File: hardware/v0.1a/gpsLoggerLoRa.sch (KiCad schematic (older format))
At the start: 34 parts, among them P1 USB_OTG, P2 CONN_01X02, Q2 FG6943010R, SW1 SW_PUSH, U2 MCP73812, U6 TPS78230

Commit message: Fixing up some errors after shuffle of libraries.
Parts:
- removed C11, C14, C6, C9: 100n, Capacitors_SMD:C_0603, symbol device:C
- removed C15, C16, C17: 1uF, Capacitors_SMD:C_0603, symbol device:C
- removed C2, C3: 22p, Capacitors_SMD:C_0603, symbol device:C
- removed D1, D2: Led_RGB_CA, footprints:LITEON_RGB, symbol gpsLogger-rescue:Led_RGB_CA
- removed FB1: 1k FB, Resistors_SMD:R_0603, symbol gpsLogger-rescue:FILTER
- removed P1: USB_OTG, footprints:USB_VERT, symbol gpsLogger-rescue:USB_OTG
- removed P2: CONN_01X02, footprints:BM02B-GHS-TBT, symbol gpsLogger-rescue:CONN_01X02
- removed Q2: FG6943010R, TO_SOT_Packages_SMD:SC-70-6, symbol gpsLogger:FG6943010R
- removed R1, R2: 27R, Resistors_SMD:R_0603, symbol device:R
- removed R10, R16, R17, R18, R19, R20, R21, R7: 1k, Resistors_SMD:R_0603, symbol device:R
- removed R12, R15: 10k, Resistors_SMD:R_0603, symbol device:R
- removed R13, R14: 100k, Resistors_SMD:R_0603, symbol device:R
- removed SW1: SW_PUSH, cameraTrigger_rev1_0:EVQ_switch, symbol gpsLogger-rescue:SW_PUSH
- removed TAG1: TAG_CONNECT, lib:tag_connect, symbol gpsLogger:TAG_CONNECT
- removed U2: MCP73812, TO_SOT_Packages_SMD:SOT-23-5, symbol gpsLogger:MCP73812
- removed U6: TPS78230, TO_SOT_Packages_SMD:SOT-23-5, symbol gpsLogger:TPS78230
- added J?: USB_OTG, symbol conn:USB_OTG
- added L?: 1k, symbol device:Ferrite_Bead_Small
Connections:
- net labels removed: +3.3V, +BATT, 1v8, LED_A_B, LED_A_G, LED_A_R, LED_B_B, LED_B_G, LED_B_R, PWR_BUT, RST, SENSE_EN, TEST, USB_IN_N, USB_IN_P, VUSB, V_SENSE, ~CHG
- wire segments 106 -> 12
- no-connect marks 1 -> 0
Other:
- note removed: "TODO: Check R7 Value\n(Charge Current)"

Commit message: Changed USB connector. Updated board outline. Updates to footprints to use 3d models. Add FLASH memory.
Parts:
- removed C1: 10n, Capacitors_SMD:C_0603, symbol device:C
- removed J?: USB_OTG, symbol conn:USB_OTG
- removed L?: 1k, symbol device:Ferrite_Bead_Small
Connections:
- net labels removed: GND, USB_DATA_N, USB_DATA_P, VBUS
- wire segments 12 -> 2
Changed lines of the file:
@@
 $Descr A3 16535 11693
 encoding utf-8
-Sheet 1 2
+Sheet 1 4
 Title "gpsLoggerLora"
 Date "2018-12-27"
@@
 Comment4 "Simple GPS logger with low power features"
 $EndDescr
-Text Label 3050 2900 0    60   ~ 0
-USB_DATA_N
-Text Label 3050 2800 0    60   ~ 0
-USB_DATA_P
 $Sheet
-S 3900 2400 2650 3400
+S 6600 2400 2650 3400
 U 5C2B8DA0
 F0 "SAMR34" 60
 F1 "SAMR34.sch" 60
-F2 "USB_DATA_N" I L 3900 2900 60
-F3 "USB_DATA_P" I L 3900 2800 60
+F2 "USB_DATA_N" I L 6600 2900 60
+F3 "USB_DATA_P" I L 6600 2800 60
+$EndSheet
+$Sheet
+S 3750 2400 2150 2150
+U 5C25E3B0
+F0 "USB" 60
+F1 "USB.sch" 60
+F2 "USB_DATA_P" I R 5900 2800 60
+F3 "USB_DATA_N" I R 5900 2900 60
+F4 "CHARGE_STAT" I R 5900 3100 60
 $EndSheet
 Wire Wire Line
-	3000 2250 3400 2250
-Text Label 3400 2250 2    60   ~ 0
-VBUS
-$Comp
-L device:C C1
-U 1 1 5691D5EA
-P 2600 3450
-F 0 "C1" H 2625 3550 50  0000 L CNN
-F 1 "10n" H 2625 3350 50  0000 L CNN
-F 2 "Capacitors_SMD:C_0603" H 2638 3300 30  0001 C CNN
-F 3 "" H 2600 3450 60  0000 C CNN
-	1    2600 3450
-	1    0    0    -1
-$EndComp
-$Comp
-L conn:USB_OTG J?
-U 1 1 5C24E04F
-P 2050 2800
-F 0 "J?" H 2105 3267 50  0000 C CNN
-F 1 "USB_OTG" H 2105 3176 50  0000 C CNN
-F 2 "" H 2200 2750 50  0001 C CNN
-F 3 "" H 2200 2750 50  0001 C CNN
-	1    2050 2800
-	1    0    0    -1
-$EndComp
-$Comp
-L device:Ferrite_Bead_Small L?
-U 1 1 5C25683B
-P 2900 2250
-F 0 "L?" V 2663 2250 50  0000 C CNN
-F 1 "1k" V 2754 2250 50  0000 C CNN
-F 2 "" V 2830 2250 50  0001 C CNN
-F 3 "~" H 2900 2250 50  0001 C CNN
-	1    2900 2250
-	0    1    1    0
-$EndComp
+	5900 2800 6600 2800
 Wire Wire Line
-	2350 2600 2600 2600
-Wire Wire Line
-	2600 2600 2600 2250
-Wire Wire Line
-	2600 2250 2800 2250
-Wire Wire Line
-	2350 2800 3900 2800
-Wire Wire Line
-	2350 2900 3900 2900
-Wire Wire Line
-	2600 3300 2600 2600
-Connection ~ 2600 2600
-$Comp
-L power:GND #PWR?
-U 1 1 5C53E1A5
-P 2600 3700
-F 0 "#PWR?" H 2600 3450 50  0001 C CNN
-F 1 "GND" H 2603 3574 50  0000 C CNN
-F 2 "" H 2500 3350 50  0001 C CNN
-F 3 "" H 2600 3700 50  0001 C CNN
-	1    2600 3700
-	1    0    0    -1
-$EndComp
-Wire Wire Line
-	2600 3700 2600 3600
-$Comp
-L power:GND #PWR?
-U 1 1 5C53E215
-P 2050 3700
-F 0 "#PWR?" H 2050 3450 50  0001 C CNN
-F 1 "GND" H 2053 3574 50  0000 C CNN
-F 2 "" H 1950 3350 50  0001 C CNN
-F 3 "" H 2050 3700 50  0001 C CNN
-	1    2050 3700
-	1    0    0    -1
-$EndComp
-Wire Wire Line
-	1950 3200 1950 3350
-Wire Wire Line
-	1950 3350 2050 3350
-Wire Wire Line
-	2050 3350 2050 3700
-Wire Wire Line
-	2050 3200 2050 3350
-Connection ~ 2050 3350
+	6600 2900 5900 2900
+$Sheet
+S 9500 2400 2850 3400
+U 5C4D6439
+F0 "memio" 60
+F1 "memio.sch" 60
+$EndSheet
 $EndSCHEMATC

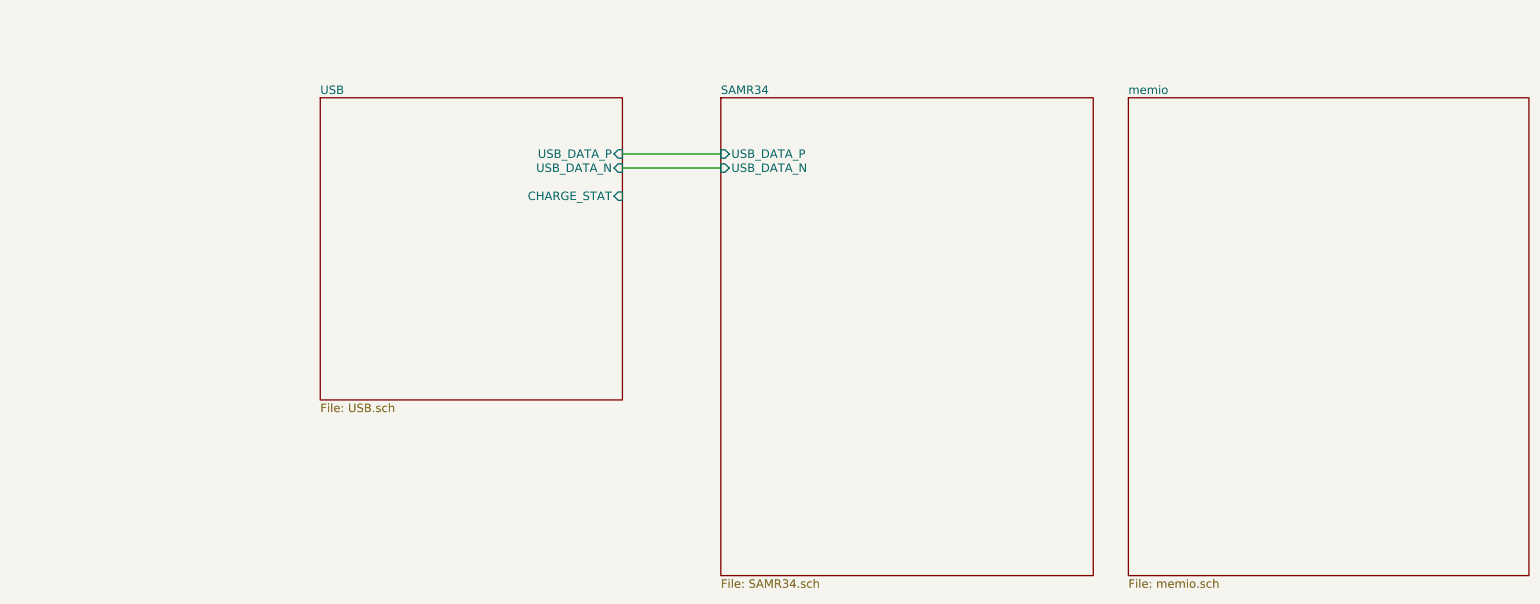
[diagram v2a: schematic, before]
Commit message: First pass schematic done. Begin routing main board.
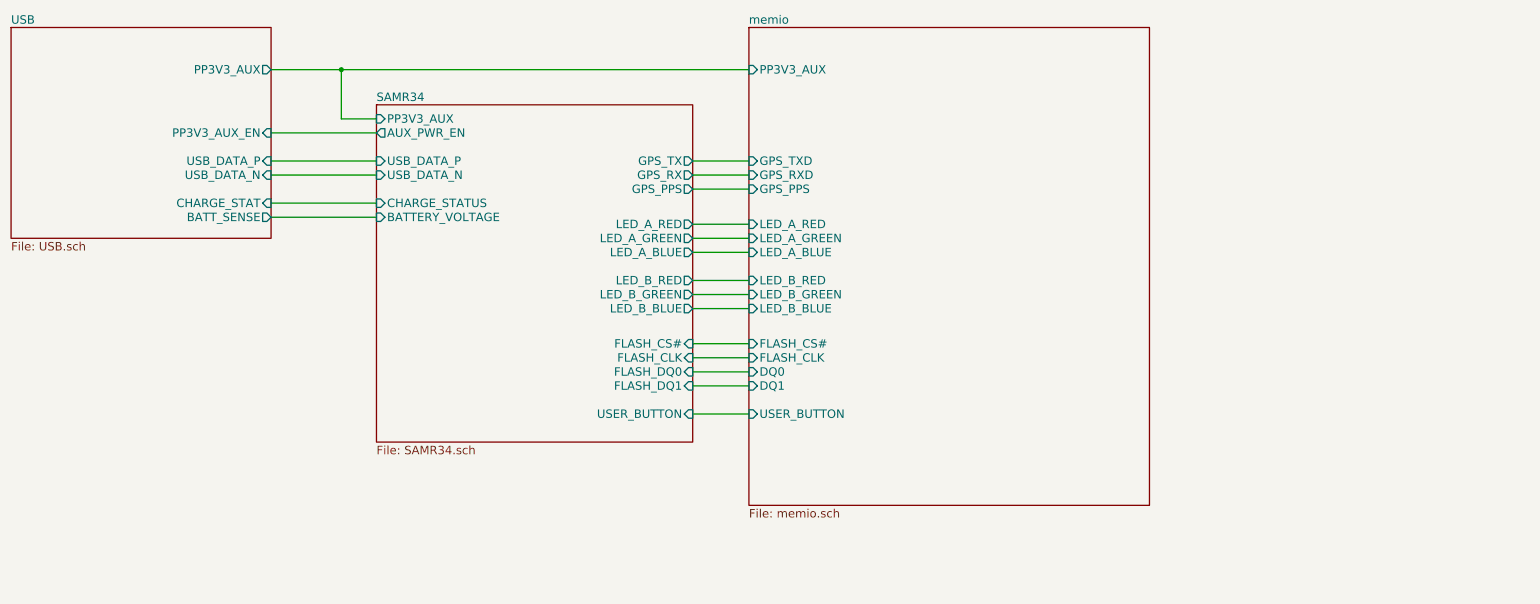
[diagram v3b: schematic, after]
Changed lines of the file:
@@
 EELAYER 26 0
 EELAYER END
-$Descr A3 16535 11693
+$Descr A4 11693 8268
 encoding utf-8
 Sheet 1 4
@@
 $EndDescr
 $Sheet
-S 6600 2400 2650 3400
+S 4150 2450 2250 2400
 U 5C2B8DA0
 F0 "SAMR34" 60
 F1 "SAMR34.sch" 60
-F2 "USB_DATA_N" I L 6600 2900 60
-F3 "USB_DATA_P" I L 6600 2800 60
+F2 "USB_DATA_N" I L 4150 2950 60
+F3 "USB_DATA_P" I L 4150 2850 60
+F4 "GPS_TX" O R 6400 2850 60
+F5 "GPS_RX" O R 6400 2950 60
+F6 "GPS_PPS" O R 6400 3050 60
+F7 "LED_A_RED" O R 6400 3300 60
+F8 "LED_A_GREEN" O R 6400 3400 60
+F9 "LED_A_BLUE" O R 6400 3500 60
+F10 "LED_B_RED" O R 6400 3700 60
+F11 "LED_B_GREEN" O R 6400 3800 60
+F12 "LED_B_BLUE" O R 6400 3900 60
+F13 "AUX_PWR_EN" O L 4150 2650 60
+F14 "FLASH_CS#" I R 6400 4150 60
+F15 "FLASH_DQ0" I R 6400 4350 60
+F16 "FLASH_DQ1" I R 6400 4450 60
+F17 "FLASH_CLK" I R 6400 4250 60
+F18 "USER_BUTTON" I R 6400 4650 60
+F19 "CHARGE_STATUS" I L 4150 3150 60
+F20 "BATTERY_VOLTAGE" I L 4150 3250 60
+F21 "PP3V3_AUX" I L 4150 2550 60
 $EndSheet
 $Sheet
-S 3750 2400 2150 2150
+S 1550 1900 1850 1500
 U 5C25E3B0
 F0 "USB" 60
 F1 "USB.sch" 60
-F2 "USB_DATA_P" I R 5900 2800 60
-F3 "USB_DATA_N" I R 5900 2900 60
-F4 "CHARGE_STAT" I R 5900 3100 60
+F2 "USB_DATA_P" I R 3400 2850 60
+F3 "USB_DATA_N" I R 3400 2950 60
+F4 "CHARGE_STAT" I R 3400 3150 60
+F5 "PP3V3_AUX_EN" I R 3400 2650 60
+F6 "PP3V3_AUX" O R 3400 2200 60
+F7 "BATT_SENSE" O R 3400 3250 60
 $EndSheet
 Wire Wire Line
-	5900 2800 6600 2800
+	3400 2850 4150 2850
 Wire Wire Line
-	6600 2900 5900 2900
+	4150 2950 3400 2950
+Wire Wire Line
+	6400 2850 6800 2850
+Wire Wire Line
+	6400 2950 6800 2950
+Wire Wire Line
+	6400 3050 6800 3050
+Wire Wire Line
+	6400 3300 6800 3300
+Wire Wire Line
+	6400 3400 6800 3400
+Wire Wire Line
+	6400 3500 6800 3500
+Wire Wire Line
+	6400 3700 6800 3700
+Wire Wire Line
+	6400 3800 6800 3800
+Wire Wire Line
+	6400 3900 6800 3900
+Wire Wire Line
+	4150 2650 3400 2650
 $Sheet
-S 9500 2400 2850 3400
+S 6800 1900 2850 3400
 U 5C4D6439
 F0 "memio" 60
 F1 "memio.sch" 60
+F2 "GPS_TXD" I L 6800 2850 60
+F3 "GPS_RXD" I L 6800 2950 60
+F4 "GPS_PPS" I L 6800 3050 60
+F5 "LED_A_RED" I L 6800 3300 60
+F6 "LED_A_GREEN" I L 6800 3400 60
+F7 "LED_A_BLUE" I L 6800 3500 60
+F8 "LED_B_RED" I L 6800 3700 60
+F9 "LED_B_GREEN" I L 6800 3800 60
+F10 "LED_B_BLUE" I L 6800 3900 60
+F11 "DQ0" I L 6800 4350 60
+F12 "DQ1" I L 6800 4450 60
+F13 "FLASH_CLK" I L 6800 4250 60
+F14 "FLASH_CS#" I L 6800 4150 60
+F15 "PP3V3_AUX" I L 6800 2200 60
+F16 "USER_BUTTON" I L 6800 4650 60
 $EndSheet
+Wire Wire Line
+	6800 2200 3900 2200
+Wire Wire Line
+	6400 4450 6800 4450
+Wire Wire Line
+	6800 4350 6400 4350
+Wire Wire Line
+	6400 4250 6800 4250
+Wire Wire Line
+	6800 4150 6400 4150
+Wire Wire Line
+	6400 4650 6800 4650
+Wire Wire Line
+	4150 2550 3900 2550
+Wire Wire Line
+	3900 2550 3900 2200
+Connection ~ 3900 2200
+Wire Wire Line
+	3900 2200 3400 2200
+Wire Wire Line
+	4150 3250 3400 3250
+Wire Wire Line
+	3400 3150 4150 3150
 $EndSCHEMATC

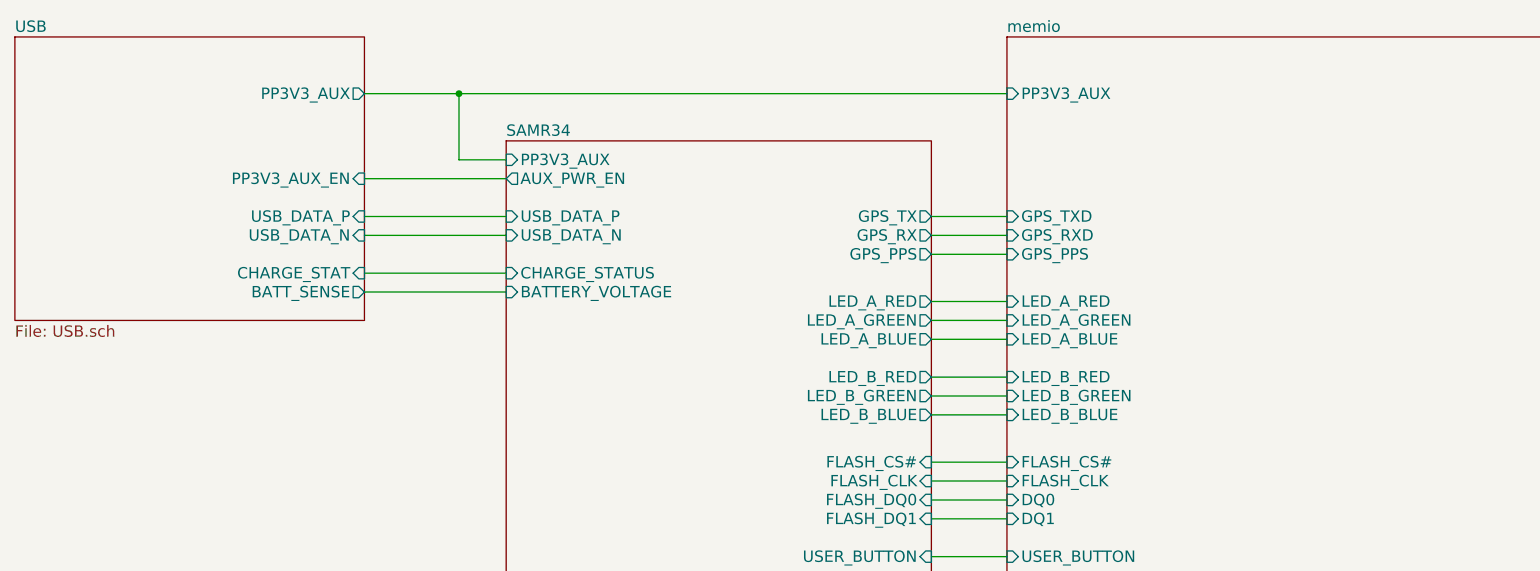
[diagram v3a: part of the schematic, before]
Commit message: Small updates to the layout. Fixed up power planes. Passed DRC
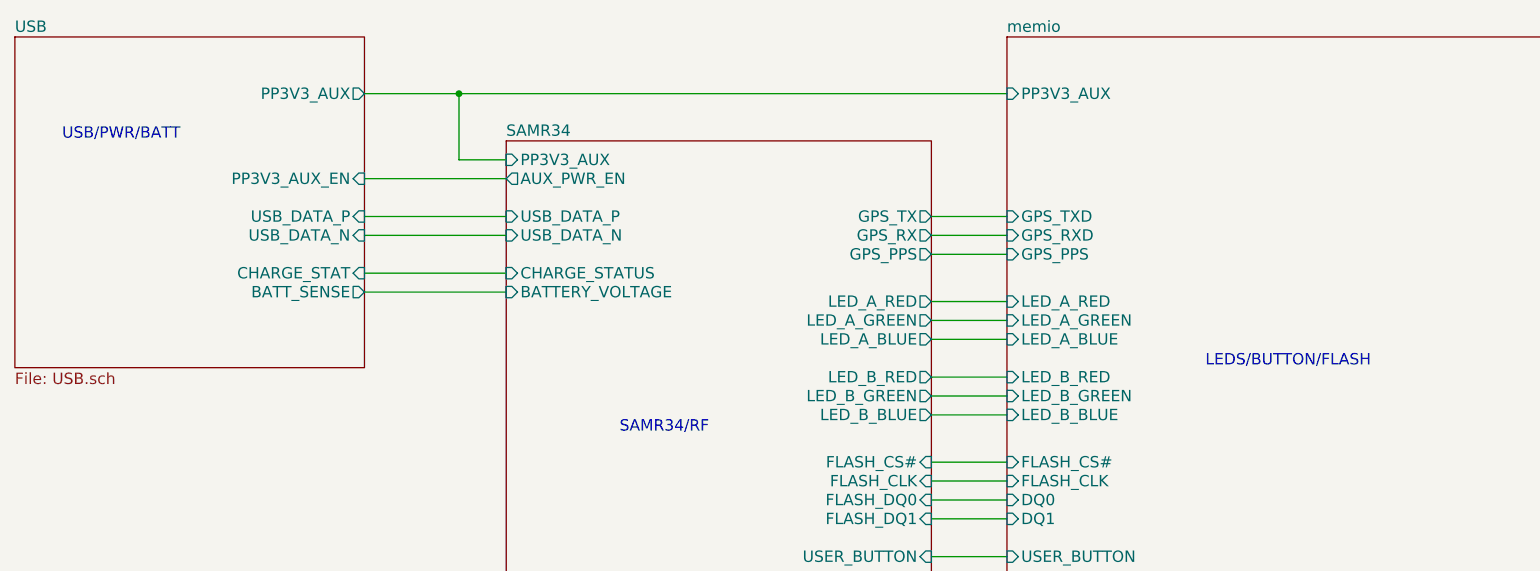
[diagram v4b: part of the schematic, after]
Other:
- note added: "LEDS/BUTTON/FLASH"
- note added: "SAMR34/RF"
- note added: "USB/PWR/BATT"
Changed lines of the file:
@@
 Sheet 1 4
 Title "gpsLoggerLora"
-Date "2018-12-27"
+Date "2018-12-29"
 Rev "v0.1a"
 Comp "Gregory S Davill"
@@
 $EndSheet
 $Sheet
-S 1550 1900 1850 1500
+S 1550 1900 1850 1750
 U 5C25E3B0
 F0 "USB" 60
@@
 Wire Wire Line
 	3400 3150 4150 3150
+Text Notes 1800 2450 0    60   ~ 0
+USB/PWR/BATT
+Text Notes 4750 4000 0    60   ~ 0
+SAMR34/RF
+Text Notes 7850 3650 0    60   ~ 0
+LEDS/BUTTON/FLASH
 $EndSCHEMATC
